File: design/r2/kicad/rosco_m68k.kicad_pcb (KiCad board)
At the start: 4 copper layers, 160 x 100 mm, 88 parts, among them IC1 MC68010P10, IC15 555N, IC2 ATF16V8BQL-15PU, IC3 ATF22V10C, IC4 XR68C681CJTR-F, IC5 ATF16V8BQL-15PU, IC6 ATF22V10C, J1 UART_A, J2 UART_B, J3 Conn_02x32_Odd_Even, J4 Conn_01x06, J5 PWR, J6 Conn_01x04_Male, Q1 Crystal, Q2 5H8ET-10.000, U1 SST39SF040, U2 SST39SF040, U3 AS6C4008-55PCN, U4 AS6C4008-55PCN

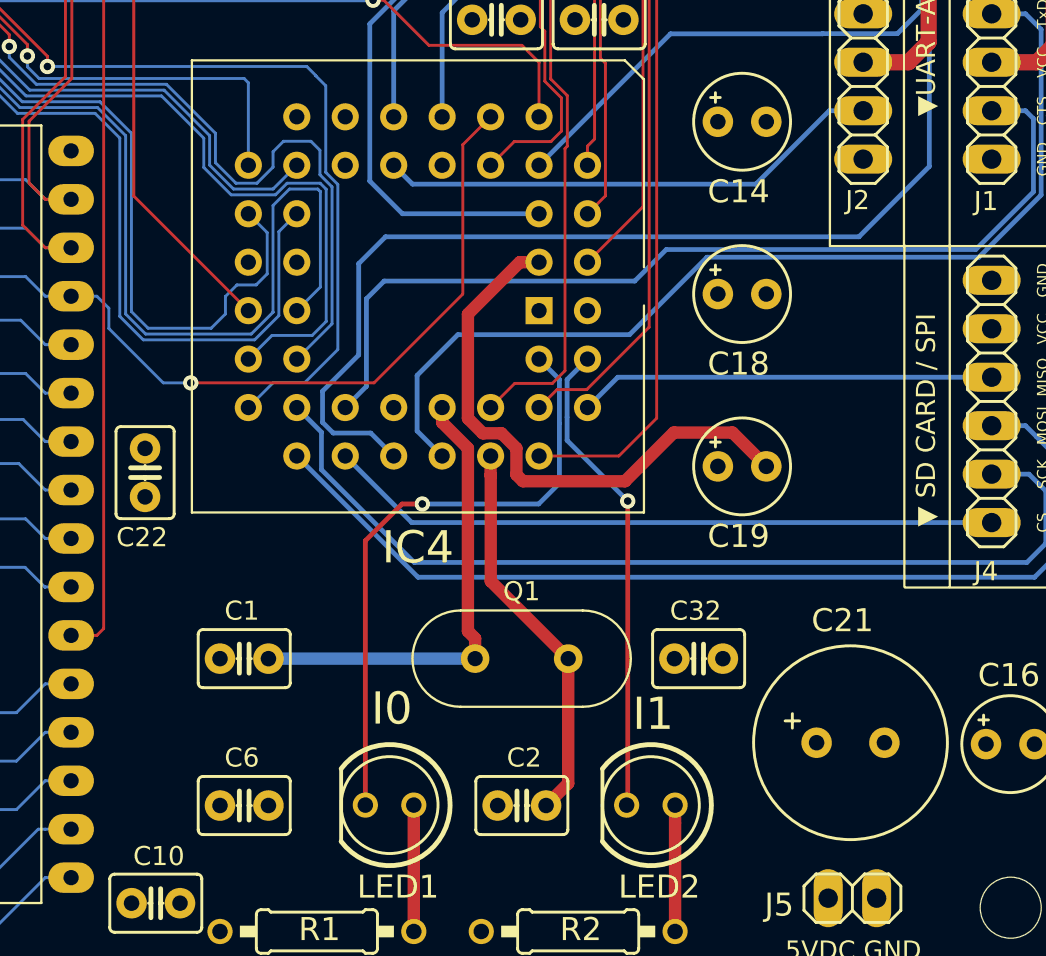
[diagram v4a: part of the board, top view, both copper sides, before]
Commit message: Fix incorrect LED hookup and add SPICS2 at @wbond's suggestion
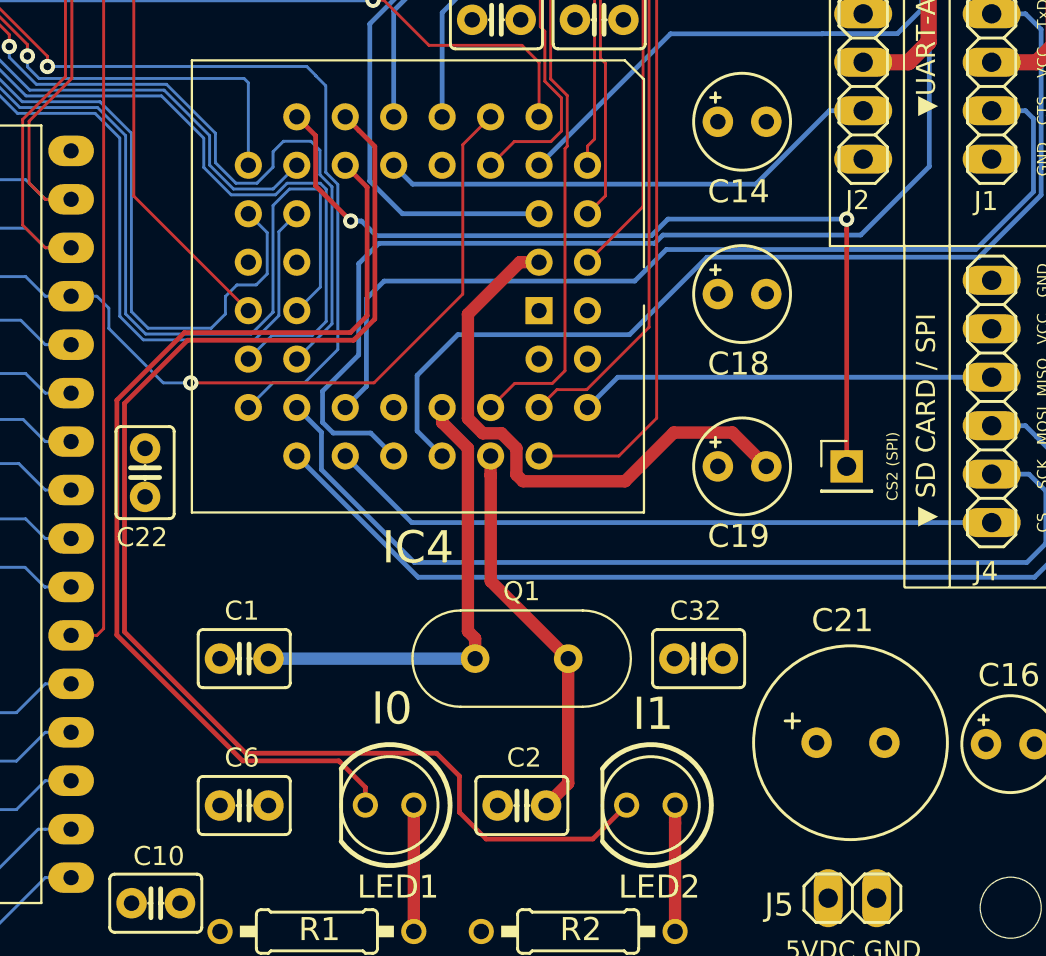
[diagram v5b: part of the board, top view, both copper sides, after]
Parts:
- added J7: Conn_01x01_Male, Connector_PinHeader_2.54mm:PinHeader_1x01_P2.54mm_Vertical, F.Cu at (215.7, 128.4)
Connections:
- IC4 pad 17: Net-(IC4-Pad17) -> SPICS2
- LED1 pad K: Net-(IC4-Pad43) -> Net-(IC4-Pad16)
- LED2 pad K: Net-(IC4-Pad42) -> Net-(IC4-Pad15)
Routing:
- net Net-(IC4-Pad15): track 0.00 -> 70.8 mm
- net Net-(IC4-Pad16): track 0.00 -> 52.9 mm
- net SPICS2: track 0.00 -> 46.3 mm, vias 0 -> 2
- net Net-(IC4-Pad43): track 32.2 -> 0.00 mm, vias 1 -> 0
- net Net-(IC4-Pad42): track 25.2 -> 0.00 mm, vias 1 -> 0
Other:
- board text added: "CS2 (SPI)"

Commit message: Fix incorrect GAL value and redo BOM etc
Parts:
- IC2, IC5: value ATF16V8BQL-15PU -> ATF22V10C
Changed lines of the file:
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@@
       (effects (font (size 1 1) (thickness 0.15)))
     )
-    (fp_text value ATF16V8BQL-15PU (at 3.81 30.27 90) (layer F.Fab)
+    (fp_text value ATF22V10C (at 3.81 30.27 90) (layer F.Fab)
       (effects (font (size 1 1) (thickness 0.15)))
     )
@@
       (effects (font (size 1 1) (thickness 0.15)))
     )
-    (fp_text value ATF16V8BQL-15PU (at 3.81 30.27) (layer F.Fab)
-      (effects (font (size 1 1) (thickness 0.15)))
-    )
+    (fp_text value ATF22V10C (at 3.81 30.27) (layer F.Fab)
+      (effects (font (size 1 1) (thickness 0.15)))
+    )

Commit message: Fix CTS/RTS labelling
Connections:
- IC4 pad 14: CTSB -> RTSB
- IC4 pad 32: CTSA -> RTSA
- IC4 pad 5: RTSB -> CTSB
- IC4 pad 8: RTSA -> CTSA
- J1 pad 2: CTSA -> RTSA
- J1 pad 6: RTSA -> CTSA
- J2 pad 2: CTSB -> RTSB
- J2 pad 6: RTSB -> CTSB
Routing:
- net RTSB: track 46.0 -> 26.6 mm
- net CTSB: track 26.6 -> 46.0 mm
- net RTSA: track 31.5 -> 49.7 mm
- net CTSA: track 49.7 -> 31.5 mm
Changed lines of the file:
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@@
       (net 100 "Net-(IC4-Pad34)"))
     (pad 32 thru_hole circle (at 5.08 10.16 270) (size 1.4224 1.4224) (drill 0.8) (layers *.Cu *.Mask)
-      (net 101 CTSA))
+      (net 109 RTSA))
     (pad 30 thru_hole circle (at 5.08 12.7 270) (size 1.4224 1.4224) (drill 0.8) (layers *.Cu *.Mask)
       (net 102 SPICLK))
@@
       (net 106 "Net-(IC4-Pad16)"))
     (pad 14 thru_hole circle (at -7.62 7.62 270) (size 1.4224 1.4224) (drill 0.8) (layers *.Cu *.Mask)
-      (net 107 CTSB))
+      (net 111 RTSB))
     (pad 12 thru_hole circle (at -7.62 5.08 270) (size 1.4224 1.4224) (drill 0.8) (layers *.Cu *.Mask)
       (net 108 "Net-(IC4-Pad12)"))
@@
       (net 4 DTACK))
     (pad 8 thru_hole circle (at -7.62 0 270) (size 1.4224 1.4224) (drill 0.8) (layers *.Cu *.Mask)
-      (net 109 RTSA))
+      (net 101 CTSA))
     (pad 42 thru_hole circle (at 2.54 -2.54 270) (size 1.4224 1.4224) (drill 0.8) (layers *.Cu *.Mask)
       (net 142 "Net-(IC4-Pad42)"))
@@
       (net 143 "Net-(IC4-Pad43)"))
     (pad 5 thru_hole circle (at -5.08 0 270) (size 1.4224 1.4224) (drill 0.8) (layers *.Cu *.Mask)
-      (net 111 RTSB))
+      (net 107 CTSB))
     (pad 3 thru_hole circle (at -2.54 0 270) (size 1.4224 1.4224) (drill 0.8) (layers *.Cu *.Mask)
       (net 18 GND))
@@
       (net 104 TXDB) (solder_mask_margin 0.1016))
     (pad 6 thru_hole oval (at 8.89 0 180) (size 3.048 1.524) (drill 1.016) (layers *.Cu *.Mask)
-      (net 111 RTSB) (solder_mask_margin 0.1016))
+      (net 107 CTSB) (solder_mask_margin 0.1016))
     (pad 4 thru_hole oval (at 3.81 0 180) (size 3.048 1.524) (drill 1.016) (layers *.Cu *.Mask)
       (net 105 RXDB) (solder_mask_margin 0.1016))
@@
       (net 137 VCCUB) (solder_mask_margin 0.1016))
     (pad 2 thru_hole oval (at -1.27 0 180) (size 3.048 1.524) (drill 1.016) (layers *.Cu *.Mask)
-      (net 107 CTSB) (solder_mask_margin 0.1016))
+      (net 111 RTSB) (solder_mask_margin 0.1016))
     (pad 1 thru_hole oval (at -3.81 0 180) (size 3.048 1.524) (drill 1.016) (layers *.Cu *.Mask)
       (net 18 GND) (solder_mask_margin 0.1016))
@@
       (net 97 TXDA) (solder_mask_margin 0.1016))
     (pad 6 thru_hole oval (at 8.89 0 180) (size 3.048 1.524) (drill 1.016) (layers *.Cu *.Mask)
-      (net 109 RTSA) (solder_mask_margin 0.1016))
+      (net 101 CTSA) (solder_mask_margin 0.1016))
     (pad 4 thru_hole oval (at 3.81 0 180) (size 3.048 1.524) (drill 1.016) (layers *.Cu *.Mask)
       (net 96 RXDA) (solder_mask_margin 0.1016))
@@
       (net 136 VCCUA) (solder_mask_margin 0.1016))
     (pad 2 thru_hole oval (at -1.27 0 180) (size 3.048 1.524) (drill 1.016) (layers *.Cu *.Mask)
-      (net 101 CTSA) (solder_mask_margin 0.1016))
+      (net 109 RTSA) (solder_mask_margin 0.1016))
     (pad 1 thru_hole oval (at -3.81 0 180) (size 3.048 1.524) (drill 1.016) (layers *.Cu *.Mask)
       (net 18 GND) (solder_mask_margin 0.1016))
@@
   (segment (start 203.701 123.69) (end 202.112 125.279) (width 0.25) (layer Bottom) (net 99))
   (segment (start 223.3 123.69) (end 203.701 123.69) (width 0.25) (layer Bottom) (net 99))
-  (segment (start 190.52041 124.17059) (end 189.412 125.279) (width 0.25) (layer Bottom) (net 101))
-  (segment (start 204.588399 118.647601) (end 191.453399 118.647601) (width 0.25) (layer Bottom) (net 101))
-  (segment (start 206.24041 116.99559) (end 204.588399 118.647601) (width 0.25) (layer Bottom) (net 101))
-  (segment (start 225.49059 113.972318) (end 222.467318 116.99559) (width 0.25) (layer Bottom) (net 101))
-  (segment (start 190.52041 119.58059) (end 190.52041 124.17059) (width 0.25) (layer Bottom) (net 101))
-  (segment (start 191.453399 118.647601) (end 190.52041 119.58059) (width 0.25) (layer Bottom) (net 101))
-  (segment (start 225.49059 110.13459) (end 225.49059 113.972318) (width 0.25) (layer Bottom) (net 101))
-  (segment (start 225.074 109.718) (end 225.49059 110.13459) (width 0.25) (layer Bottom) (net 101))
-  (segment (start 222.467318 116.99559) (end 206.24041 116.99559) (width 0.25) (layer Bottom) (net 101))
-  (segment (start 223.3 109.718) (end 225.074 109.718) (width 0.25) (layer Bottom) (net 101))
+  (segment (start 190.52041 124.17059) (end 189.412 125.279) (width 0.25) (layer Bottom) (net 109))
+  (segment (start 204.588399 118.647601) (end 191.453399 118.647601) (width 0.25) (layer Bottom) (net 109))
+  (segment (start 206.24041 116.99559) (end 204.588399 118.647601) (width 0.25) (layer Bottom) (net 109))
+  (segment (start 225.49059 113.972318) (end 222.467318 116.99559) (width 0.25) (layer Bottom) (net 109))
+  (segment (start 190.52041 119.58059) (end 190.52041 124.17059) (width 0.25) (layer Bottom) (net 109))
+  (segment (start 191.453399 118.647601) (end 190.52041 119.58059) (width 0.25) (layer Bottom) (net 109))
+  (segment (start 225.49059 110.13459) (end 225.49059 113.972318) (width 0.25) (layer Bottom) (net 109))
+  (segment (start 225.074 109.718) (end 225.49059 110.13459) (width 0.25) (layer Bottom) (net 109))
+  (segment (start 222.467318 116.99559) (end 206.24041 116.99559) (width 0.25) (layer Bottom) (net 109))
+  (segment (start 223.3 109.718) (end 225.074 109.718) (width 0.25) (layer Bottom) (net 109))
   (segment (start 226.138 129.653) (end 225.255 128.77) (width 0.25) (layer Bottom) (net 102))
   (segment (start 226.138 132.409) (end 226.138 129.653) (width 0.25) (layer Bottom) (net 102))
@@
   (segment (start 190.560989 113.727989) (end 189.412 112.579) (width 0.25) (layer Top) (net 106))
   (segment (start 190.560989 120.469919) (end 190.560989 113.727989) (width 0.25) (layer Top) (net 106))
-  (segment (start 210.940399 113.567601) (end 214.79 109.718) (width 0.25) (layer Bottom) (net 107))
-  (segment (start 191.952 112.579) (end 192.940601 113.567601) (width 0.25) (layer Bottom) (net 107))
-  (segment (start 192.940601 113.567601) (end 210.940399 113.567601) (width 0.25) (layer Bottom) (net 107))
-  (segment (start 214.79 109.718) (end 216.564 109.718) (width 0.25) (layer Bottom) (net 107))
-  (segment (start 214.44741 105.67741) (end 214.43782 105.687) (width 0.25) (layer Bottom) (net 109))
-  (segment (start 219.62941 104.40559) (end 218.35759 105.67741) (width 0.25) (layer Bottom) (net 109))
-  (segment (start 220.39541 99.558) (end 219.62941 100.324) (width 0.25) (layer Bottom) (net 109))
-  (segment (start 206.464 105.687) (end 199.572 112.579) (width 0.25) (layer Bottom) (net 109))
-  (segment (start 219.62941 100.324) (end 219.62941 104.40559) (width 0.25) (layer Bottom) (net 109))
-  (segment (start 218.35759 105.67741) (end 214.44741 105.67741) (width 0.25) (layer Bottom) (net 109))
-  (segment (start 223.3 99.558) (end 220.39541 99.558) (width 0.25) (layer Bottom) (net 109))
-  (segment (start 214.43782 105.687) (end 206.464 105.687) (width 0.25) (layer Bottom) (net 109))
+  (segment (start 210.940399 113.567601) (end 214.79 109.718) (width 0.25) (layer Bottom) (net 111))
+  (segment (start 191.952 112.579) (end 192.940601 113.567601) (width 0.25) (layer Bottom) (net 111))
+  (segment (start 192.940601 113.567601) (end 210.940399 113.567601) (width 0.25) (layer Bottom) (net 111))
+  (segment (start 214.79 109.718) (end 216.564 109.718) (width 0.25) (layer Bottom) (net 111))
+  (segment (start 214.44741 105.67741) (end 214.43782 105.687) (width 0.25) (layer Bottom) (net 101))
+  (segment (start 219.62941 104.40559) (end 218.35759 105.67741) (width 0.25) (layer Bottom) (net 101))
+  (segment (start 220.39541 99.558) (end 219.62941 100.324) (width 0.25) (layer Bottom) (net 101))
+  (segment (start 206.464 105.687) (end 199.572 112.579) (width 0.25) (layer Bottom) (net 101))
+  (segment (start 219.62941 100.324) (end 219.62941 104.40559) (width 0.25) (layer Bottom) (net 101))
+  (segment (start 218.35759 105.67741) (end 214.44741 105.67741) (width 0.25) (layer Bottom) (net 101))
+  (segment (start 223.3 99.558) (end 220.39541 99.558) (width 0.25) (layer Bottom) (net 101))
+  (segment (start 214.43782 105.687) (end 206.464 105.687) (width 0.25) (layer Bottom) (net 101))
   (segment (start 202.071801 124.339199) (end 205.341 121.07) (width 0.1524) (layer Top) (net 110))
   (segment (start 200.511801 124.339199) (end 202.071801 124.339199) (width 0.1524) (layer Top) (net 110))
@@
   (segment (start 195.063866 62.232) (end 193.696666 60.8648) (width 0.1524) (layer Bottom) (net 110))
   (segment (start 203.01 62.232) (end 195.063866 62.232) (width 0.1524) (layer Bottom) (net 110))
-  (segment (start 214.79 99.558) (end 212.65241 101.69559) (width 0.25) (layer Bottom) (net 111))
-  (segment (start 216.564 99.558) (end 214.79 99.558) (width 0.25) (layer Bottom) (net 111))
-  (segment (start 194.166317 101.69559) (end 190.699 105.162907) (width 0.25) (layer Bottom) (net 111))
-  (segment (start 212.65241 101.69559) (end 194.166317 101.69559) (width 0.25) (layer Bottom) (net 111))
-  (segment (start 190.699 105.162907) (end 190.699 113.409) (width 0.25) (layer Bottom) (net 111))
-  (segment (start 192.409 115.119) (end 199.572 115.119) (width 0.25) (layer Bottom) (net 111))
-  (segment (start 190.699 113.409) (end 192.409 115.119) (width 0.25) (layer Bottom) (net 111))
+  (segment (start 214.79 99.558) (end 212.65241 101.69559) (width 0.25) (layer Bottom) (net 107))
+  (segment (start 216.564 99.558) (end 214.79 99.558) (width 0.25) (layer Bottom) (net 107))
+  (segment (start 194.166317 101.69559) (end 190.699 105.162907) (width 0.25) (layer Bottom) (net 107))
+  (segment (start 212.65241 101.69559) (end 194.166317 101.69559) (width 0.25) (layer Bottom) (net 107))
+  (segment (start 190.699 105.162907) (end 190.699 113.409) (width 0.25) (layer Bottom) (net 107))
+  (segment (start 192.409 115.119) (end 199.572 115.119) (width 0.25) (layer Bottom) (net 107))
+  (segment (start 190.699 113.409) (end 192.409 115.119) (width 0.25) (layer Bottom) (net 107))
   (segment (start 195.146666 76.1048) (end 196.407866 77.366) (width 0.25) (layer Bottom) (net 116))
   (segment (start 193.696666 76.1048) (end 195.146666 76.1048) (width 0.25) (layer Bottom) (net 116))

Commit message: Bite the bullet and do IPL properly...
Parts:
- removed R4, R5, R6: 4K7, rosco_m68k:0207_10
- added IC7: 74LS148, Package_DIP:DIP-16_W7.62mm_LongPads, F.Cu at (137.8, 98.1)
- added R12: 4K7, rosco_m68k:0207_10, F.Cu at (101.7, 73.6)
- added R15: 4K7, rosco_m68k:0207_10, F.Cu at (98.7, 73.6)
- added R16: 4K7, rosco_m68k:0207_10, F.Cu at (183.0, 105.5)
- added R17: 4K7, rosco_m68k:0207_10, F.Cu at (95.8, 73.6)
- added R18: 4K7, rosco_m68k:0207_10, F.Cu at (92.8, 73.6)
- added REF**: SM-rosco_m68k_logo, rosco_m68k:SM-rosco_m68k_logo, F.Cu at (176.6, 97.6)
- REF**: moved to B.Cu
- moved REF** 76.5 mm to (85.0, 105.8), turned to 270 degrees
- moved C7 10.6 mm to (159.1, 94.3)
- moved J7 3.07 mm to (216.6, 131.3)
- moved R3 0.76 mm to (133.5, 94.0)
- moved C15 0.47 mm to (146.4, 104.9)
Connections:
- IC4 pad 24: IPL2 -> DUAIRQ
- J3 pad 14: Net-(J3-Pad14) -> IRQ3
- J3 pad 26: IPL0 -> IRQ5
- J3 pad 28: IPL1 -> IRQ2
- J3 pad 30: IPL2 -> IRQ6
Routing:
- net IPL2: track 180.3 -> 20.6 mm, vias 2 -> 1
- net IRQ2: track 0.00 -> 118.4 mm, vias 0 -> 3
- net IRQ5: track 0.00 -> 107.7 mm, vias 0 -> 3
- net IRQ6: track 0.00 -> 106.1 mm, vias 0 -> 2
- net IRQ3: track 0.00 -> 100.4 mm, vias 0 -> 3
- net IPL0: track 93.7 -> 11.0 mm
- net DUAIRQ: track 0.00 -> 70.9 mm, vias 0 -> 1
- net IPL1: track 91.4 -> 23.3 mm
- net AS: track 217.8 -> 209.9 mm, vias 5 -> 3
- net BGACK: track 115.1 -> 107.9 mm, vias 2 -> 1
- net SPICS2: track 46.3 -> 49.6 mm
- net BERR: track 184.6 -> 181.5 mm
- net FC1: track 139.4 -> 136.7 mm
- net FC0: track 133.5 -> 130.7 mm
- net FC2: track 146.2 -> 143.4 mm
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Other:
- board text added: "Revision 2.1 (November 2021)"
- board text added: "version 2"
- board text removed: "Revision 2.0 (November 2021)"
